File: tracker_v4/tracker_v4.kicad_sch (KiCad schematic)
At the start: 16 parts, among them J2 P70-7000045, J3 P70-7000045, U1 XIAO-ESP32-DIP, U2 LIS3DH, U4 INA226AIDGSR

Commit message: starting v4
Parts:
- removed J2, J3: P70-7000045, P70_7000045:HARWIN_P70-7000045, symbol P70-7000045:P70-7000045
- removed U1: XIAO-ESP32-DIP, Seeed_Studio_XIAO_Series:XIAO-ESP32-C6-DIP, symbol Seeed_Studio_XIAO_Series:XIAO-ESP32-C6-SMD
- added C?: 1u, symbol Device:C
- added R?: 10k, Resistor_SMD:R_0603_1608Metric, symbol Device:R
- added U?: ESP32-C6-MINI-1-N4, ESP32-C6-MINI-1-N4:XCVR_ESP32-C6-MINI-1-N4, symbol ESP32-C6-MINI-1-N4:ESP32-C6-MINI-1-N4
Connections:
- net 3v3: now also U?.3 (3V3)
- net GND: now also C?.2, U?.1 (GND1), U?.11 (GND1), U?.14 (GND1), U?.2 (GND1), U?.36 (GND1), U?.37 (GND1), U?.38 (GND1), U?.39 (GND1), U?.40 (GND1), U?.41 (GND1), U?.42 (GND1), U?.43 (GND1), U?.44 (GND1), U?.45 (GND1), U?.46 (GND1), U?.47 (GND2), U?.48 (GND2), U?.49_1 (GND2), U?.49_2 (GND2), U?.49_3 (GND2), U?.49_4 (GND2), U?.49_5 (GND2), U?.49_6 (GND2), U?.49_7 (GND2), U?.49_8 (GND2), U?.49_9 (GND2), U?.50 (GND2), U?.51 (GND2), U?.52 (GND2), U?.53 (GND2)
- net at TP5.1, U2.11 (INT1): now also R?.2
- new net: C?.1, R?.1, U?.8 (EN)
- new net: U?.21 (NC), U?.32 (NC), U?.33 (NC), U?.34 (NC), U?.35 (NC), U?.4 (NC), U?.7 (NC)
- no-connect marks 21 -> 4
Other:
- sheet Charging_and_Battery ports: added USB_DM, USB_DP; removed none

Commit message: added some stuff to schematic
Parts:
- added C?: 10u, symbol Device:C
- added IC?: RT9080-33GJ5, RT9080-33GJ5:SOT94P280X100-5N, symbol RT9080-33GJ5:RT9080-33GJ5
- added R11: 10k, symbol Device:R
- added R?: 4.7k, Resistor_SMD:R_0603_1608Metric, symbol Device:R
- added SW?: SW_Push, symbol Switch:SW_Push
- gave numbers to parts that had none: 3
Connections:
- net 3v3: now also R12.2, TP5.1, IC?.5 (VOUT), R11.1, R?.1
- net GND: now also C?.2, IC?.2 (GND), IC?.4 (SNS), SW?.1
- net SCL: now also U1.29 (IO23)
- net SDA: now also U1.28 (IO22)
- net INA226_ALERT: now reaches U4.3 (Alert)
- net INA226_ALERT: now also U1.12 (IO0), R?.2
- net USB_DM: now reaches U1.17 (IO12)
- net USB_DP: now reaches U1.18 (IO13)
- net at U1.22 (IO8): now also R11.2
- net at U1.23 (IO9): now also SW?.2
- net LIS3DH_INT1: now reaches U1.5 (IO2)
- net LIS3DH_INT1: now also U2.11 (INT1)
- net Shunt_Output renamed SHUNT_OUTPUT
- net SHUNT_OUTPUT: now also C?.1, IC?.1 (VIN), IC?.3 (EN)
- no-connect marks 4 -> 18
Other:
- moved on the sheet: C4, TP3, TP4, TP5, U1

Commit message: found changed netlist
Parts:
- gave numbers to parts that had none: 4
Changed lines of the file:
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@@
 		(dnp no)
 		(fields_autoplaced yes)
-		(property "Reference" "R?"
+		(property "Reference" "R13"
 			(at 111.76 38.0999 0)
 			(show_name no)
@@
 			(project "tracker_v4"
 				(path "/0704e846-b6bf-4206-baa8-1088b529855e"
-					(reference "R?")
+					(reference "R13")
 					(unit 1)
 				)
@@
 		(dnp no)
 		(fields_autoplaced yes)
-		(property "Reference" "C?"
+		(property "Reference" "C8"
 			(at 31.75 102.8699 0)
 			(show_name no)
@@
 			(project "tracker_v4"
 				(path "/0704e846-b6bf-4206-baa8-1088b529855e"
-					(reference "C?")
+					(reference "C8")
 					(unit 1)
 				)
@@
 		(dnp no)
 		(fields_autoplaced yes)
-		(property "Reference" "IC?"
+		(property "Reference" "IC1"
 			(at 53.34 87.63 0)
 			(show_name no)
@@
 			(project "tracker_v4"
 				(path "/0704e846-b6bf-4206-baa8-1088b529855e"
-					(reference "IC?")
+					(reference "IC1")
 					(unit 1)
 				)
@@
 		(dnp no)
 		(fields_autoplaced yes)
-		(property "Reference" "SW?"
+		(property "Reference" "SW1"
 			(at 146.05 106.6799 90)
 			(show_name no)
@@
 			(project "tracker_v4"
 				(path "/0704e846-b6bf-4206-baa8-1088b529855e"
-					(reference "SW?")
-					(unit 1)
-				)
+					(reference "SW1")
+					(unit 1)
+				)

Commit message: m
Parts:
- added C9: 22u, symbol Device:C
- added SW2: SW_Push, Button_Switch_SMD:Nidec_Copal_CAS-120A, symbol Switch:SW_Push
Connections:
- net 3v3: now also C9.2
- net GND: now also C9.1; no longer IC1.4 (SNS)
- net at R12.1, U1.8 (EN): now also SW2.1; no longer C4.1
- new net: C4.1, SW2.2
- no-connect marks 18 -> 19

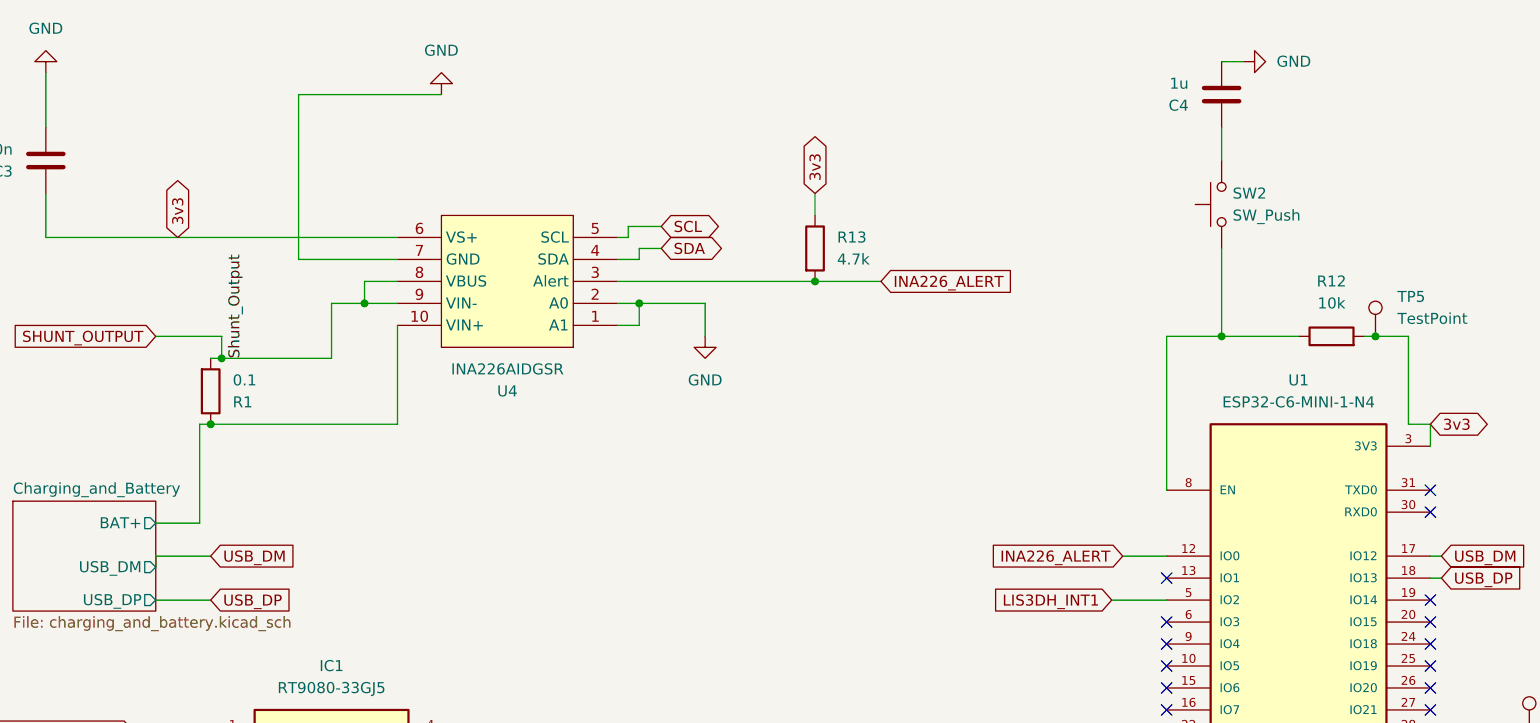
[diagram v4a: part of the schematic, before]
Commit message: added diodes
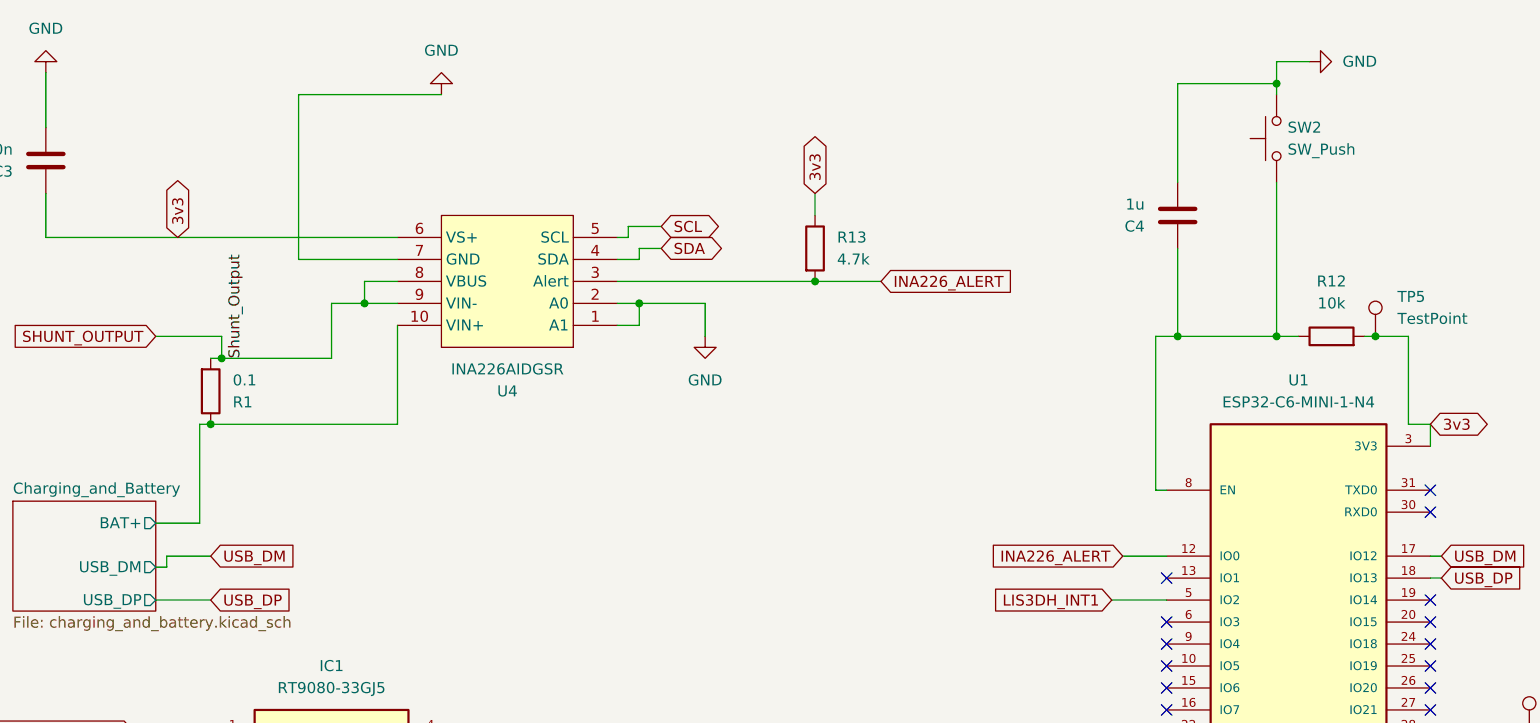
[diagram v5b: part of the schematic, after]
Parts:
- C2: footprint Capacitor_SMD:C_0603_1608Metric -> Capacitor_SMD:C_0805_2012Metric
- C4: footprint (none) -> Capacitor_SMD:C_0603_1608Metric
- C8: footprint (none) -> Capacitor_SMD:C_0201_0603Metric
- C9: footprint (none) -> Capacitor_SMD:C_1206_3216Metric
- R11: footprint (none) -> Resistor_SMD:R_0603_1608Metric
- SW1: footprint (none) -> Button_Switch_SMD:SW_Push_1P1T_NO_CK_KMR2
- SW2: footprint Button_Switch_SMD:Nidec_Copal_CAS-120A -> Button_Switch_SMD:SW_Push_1P1T_NO_CK_KMR2
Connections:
- net GND: now also SW2.2
- net at C4.1: now also R12.1, SW2.1, U1.8 (EN); no longer SW2.2
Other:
- moved on the sheet: C4, SW2
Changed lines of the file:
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@@
 	)
 	(junction
-		(at 156.21 49.53)
+		(at 173.99 49.53)
 		(diameter 0)
 		(color 0 0 0 0)
 	)
 	(junction
-		(at 173.99 49.53)
+		(at 27.94 113.03)
 		(diameter 0)
 		(color 0 0 0 0)
 	)
 	(junction
-		(at 27.94 113.03)
+		(at 196.85 101.6)
 		(diameter 0)
 		(color 0 0 0 0)
 	)
 	(junction
-		(at 196.85 101.6)
+		(at 162.56 20.32)
 		(diameter 0)
 		(color 0 0 0 0)
@@
 	)
 	(junction
+		(at 162.56 49.53)
+		(diameter 0)
+		(color 0 0 0 0)
+	)
+	(junction
 		(at 224.79 76.2)
 		(diameter 0)
@@
 	)
 	(junction
+		(at 151.13 49.53)
+		(diameter 0)
+		(color 0 0 0 0)
+	)
+	(junction
 		(at 88.9 45.72)
 		(diameter 0)
@@
 	(wire
 		(pts
+			(xy 162.56 17.78) (xy 162.56 20.32)
+		)
+		(stroke
+			(width 0)
+			(type default)
+		)
+	)
+	(wire
+		(pts
 			(xy 40.64 52.07) (xy 53.34 52.07)
 		)
@@
 	(wire
 		(pts
+			(xy 151.13 49.53) (xy 162.56 49.53)
+		)
+		(stroke
+			(width 0)
+			(type default)
+		)
+	)
+	(wire
+		(pts
 			(xy 31.75 99.06) (xy 31.75 95.25)
 		)
@@
 	(wire
 		(pts
+			(xy 151.13 31.75) (xy 151.13 20.32)
+		)
+		(stroke
+			(width 0)
+			(type default)
+		)
+	)
+	(wire
+		(pts
 			(xy 200.66 101.6) (xy 196.85 101.6)
 		)
@@
 	(wire
 		(pts
+			(xy 162.56 31.75) (xy 162.56 49.53)
+		)
+		(stroke
+			(width 0)
+			(type default)
+		)
+	)
+	(wire
+		(pts
 			(xy 57.15 45.72) (xy 60.96 45.72)
 		)
@@
 	(wire
 		(pts
+			(xy 148.59 49.53) (xy 151.13 49.53)
+		)
+		(stroke
+			(width 0)
+			(type default)
+		)
+	)
+	(wire
+		(pts
 			(xy 209.55 76.2) (xy 219.71 76.2)
 		)
@@
 	(wire
 		(pts
-			(xy 86.36 48.26) (xy 88.9 48.26)
+			(xy 34.29 76.2) (xy 34.29 74.93)
 		)
 		(stroke
@@
 	(wire
 		(pts
-			(xy 227.33 97.79) (xy 222.25 97.79)
+			(xy 86.36 48.26) (xy 88.9 48.26)
 		)
 		(stroke
@@
 	(wire
 		(pts
-			(xy 149.86 49.53) (xy 156.21 49.53)
+			(xy 227.33 97.79) (xy 222.25 97.79)
 		)
 		(stroke
@@
 	(wire
 		(pts
-			(xy 149.86 49.53) (xy 149.86 67.31)
-		)
-		(stroke
-			(width 0)
-			(type default)
-		)
-	)
-	(wire
-		(pts
 			(xy 243.84 58.42) (xy 243.84 64.77)
 		)
@@
 	(wire
 		(pts
-			(xy 33.02 74.93) (xy 33.02 76.2)
+			(xy 60.96 59.69) (xy 60.96 48.26)
 		)
 		(stroke
@@
 	(wire
 		(pts
-			(xy 60.96 59.69) (xy 60.96 48.26)
+			(xy 162.56 20.32) (xy 162.56 21.59)
 		)
 		(stroke
@@
 	(wire
 		(pts
-			(xy 156.21 39.37) (xy 156.21 49.53)
+			(xy 227.33 90.17) (xy 224.79 90.17)
 		)
 		(stroke
@@
 	(wire
 		(pts
-			(xy 227.33 90.17) (xy 224.79 90.17)
+			(xy 250.19 114.3) (xy 224.79 114.3)
 		)
 		(stroke
@@
 	(wire
 		(pts
-			(xy 250.19 114.3) (xy 224.79 114.3)
+			(xy 143.51 80.01) (xy 149.86 80.01)
 		)
 		(stroke
@@
 	(wire
 		(pts
-			(xy 143.51 80.01) (xy 149.86 80.01)
+			(xy 242.57 74.93) (xy 242.57 77.47)
 		)
 		(stroke
@@
 	(wire
 		(pts
-			(xy 242.57 74.93) (xy 242.57 77.47)
+			(xy 151.13 39.37) (xy 151.13 49.53)
 		)
 		(stroke
@@
 	(wire
 		(pts
-			(xy 156.21 25.4) (xy 156.21 29.21)
+			(xy 20.32 38.1) (xy 20.32 33.02)
 		)
 		(stroke
@@
 	(wire
 		(pts
-			(xy 20.32 38.1) (xy 20.32 33.02)
+			(xy 53.34 45.72) (xy 57.15 45.72)
 		)
 		(stroke
@@
 	(wire
 		(pts
-			(xy 53.34 45.72) (xy 57.15 45.72)
+			(xy 240.03 139.7) (xy 240.03 105.41)
 		)
 		(stroke
@@
 	(wire
 		(pts
-			(xy 240.03 139.7) (xy 240.03 105.41)
+			(xy 148.59 67.31) (xy 149.86 67.31)
 		)
 		(stroke
@@
 	(wire
 		(pts
+			(xy 34.29 74.93) (xy 39.37 74.93)
+		)
+		(stroke
+			(width 0)
+			(type default)
+		)
+	)
+	(wire
+		(pts
 			(xy 261.62 123.19) (xy 261.62 114.3)
 		)
@@
 	(wire
 		(pts
-			(xy 158.75 17.78) (xy 156.21 17.78)
+			(xy 162.56 17.78) (xy 166.37 17.78)
 		)
 		(stroke
@@
 	(wire
 		(pts
+			(xy 151.13 20.32) (xy 162.56 20.32)
+		)
+		(stroke
+			(width 0)
+			(type default)
+		)
+	)
+	(wire
+		(pts
 			(xy 87.63 36.83) (xy 91.44 36.83)
 		)
@@
 	(wire
 		(pts
-			(xy 39.37 74.93) (xy 33.02 74.93)
+			(xy 34.29 76.2) (xy 33.02 76.2)
 		)
 		(stroke
@@
 	(wire
 		(pts
-			(xy 156.21 49.53) (xy 165.1 49.53)
+			(xy 148.59 49.53) (xy 148.59 67.31)
 		)
 		(stroke
@@
 	(wire
 		(pts
+			(xy 162.56 49.53) (xy 165.1 49.53)
+		)
+		(stroke
+			(width 0)
+			(type default)
+		)
+	)
+	(wire
+		(pts
 			(xy 39.37 59.69) (xy 60.96 59.69)
 		)
@@
 			)
 		)
-		(property "Footprint" "Capacitor_SMD:C_0603_1608Metric"
+		(property "Footprint" "Capacitor_SMD:C_0805_2012Metric"
 			(at 234.6452 72.39 0)
 			(hide yes)
@@
 	(symbol
 		(lib_id "power:GND")
-		(at 158.75 17.78 90)
+		(at 166.37 17.78 90)
 		(unit 1)
 		(body_style 1)
@@
 		(fields_autoplaced yes)
 		(property "Reference" "#PWR010"
-			(at 165.1 17.78 0)
+			(at 172.72 17.78 0)
 			(hide yes)
 			(show_name no)
@@
 		)
 		(property "Value" "GND"
-			(at 162.56 17.7801 90)
+			(at 170.18 17.7801 90)
 			(show_name no)
 			(do_not_autoplace no)
@@
 		)
 		(property "Footprint" ""
-			(at 158.75 17.78 0)
+			(at 166.37 17.78 0)
 			(hide yes)
 			(show_name no)
@@
 		)
 		(property "Datasheet" ""
-			(at 158.75 17.78 0)
+			(at 166.37 17.78 0)
 			(hide yes)
 			(show_name no)
@@
 		)
 		(property "Description" "Power symbol creates a global label with name \"GND\" , ground"
-			(at 158.75 17.78 0)
+			(at 166.37 17.78 0)
 			(hide yes)
 			(show_name no)
@@
 			)
 		)
-		(property "Footprint" ""
+		(property "Footprint" "Capacitor_SMD:C_0201_0603Metric"
 			(at 28.9052 107.95 0)
 			(hide yes)
@@
 			)
 		)
-		(property "Footprint" ""
+		(property "Footprint" "Resistor_SMD:R_0603_1608Metric"
 			(at 138.938 106.68 90)
 			(hide yes)
@@
 			)
 		)
-		(property "Footprint" ""
+		(property "Footprint" "Capacitor_SMD:C_1206_3216Metric"
 			(at 220.6752 66.04 0)
 			(hide yes)
@@
 			(at 219.71 62.23 0)
 			(hide yes)
-			(show_name no)
+			(show_name yes)
 			(do_not_autoplace no)
 			(effects
@@
 	(symbol
 		(lib_id "Device:C")
-		(at 156.21 21.59 180)
+		(at 151.13 35.56 180)
 		(unit 1)
 		(body_style 1)
@@
 		(fields_autoplaced yes)
 		(property "Reference" "C4"
-			(at 152.4 22.8601 0)
+			(at 147.32 36.8301 0)
 			(show_name no)
 			(do_not_autoplace no)
@@
 		)
 		(property "Value" "1u"
-			(at 152.4 20.3201 0)
+			(at 147.32 34.2901 0)
 			(show_name no)
 			(do_not_autoplace no)
@@
 			)
 		)
-		(property "Footprint" ""
-			(at 155.2448 17.78 0)
+		(property "Footprint" "Capacitor_SMD:C_0603_1608Metric"
+			(at 150.1648 31.75 0)
 			(hide yes)
 			(show_name no)
@@
 		)
 		(property "Datasheet" ""
-			(at 156.21 21.59 0)
+			(at 151.13 35.56 0)
 			(hide yes)
 			(show_name no)
@@
 		)
 		(property "Description" "Unpolarized capacitor"
-			(at 156.21 21.59 0)
+			(at 151.13 35.56 0)
 			(hide yes)
 			(show_name no)
@@
 			)
 		)
-		(property "Footprint" ""
+		(property "Footprint" "Button_Switch_SMD:SW_Push_1P1T_NO_CK_KMR2"
 			(at 139.7 107.95 0)
 			(hide yes)
@@
 	(symbol
 		(lib_id "Switch:SW_Push")
-		(at 156.21 34.29 90)
+		(at 162.56 26.67 90)
 		(unit 1)
 		(body_style 1)
@@
 		(fields_autoplaced yes)
 		(property "Reference" "SW2"
-			(at 157.48 33.0199 90)
+			(at 163.83 25.3999 90)
 			(show_name no)
 			(do_not_autoplace no)
@@
 		)
 		(property "Value" "SW_Push"
-			(at 157.48 35.5599 90)
+			(at 163.83 27.9399 90)
 			(show_name no)
 			(do_not_autoplace no)
@@
 			)
 		)
-		(property "Footprint" "Button_Switch_SMD:Nidec_Copal_CAS-120A"
-			(at 151.13 34.29 0)
+		(property "Footprint" "Button_Switch_SMD:SW_Push_1P1T_NO_CK_KMR2"
+			(at 157.48 26.67 0)
 			(hide yes)
 			(show_name no)
@@
 		)
 		(property "Datasheet" ""
-			(at 151.13 34.29 0)
+			(at 157.48 26.67 0)
 			(hide yes)
 			(show_name no)
@@
 		)
 		(property "Description" "Push button switch, generic, two pins"
-			(at 156.21 34.29 0)
+			(at 162.56 26.67 0)
 			(hide yes)
 			(show_name no)

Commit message: corrected schematic
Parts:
- C8: footprint Capacitor_SMD:C_0201_0603Metric -> Capacitor_SMD:C_0805_2012Metric
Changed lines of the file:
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@@
 			)
 		)
-		(property "Footprint" "Capacitor_SMD:C_0201_0603Metric"
+		(property "Footprint" "Capacitor_SMD:C_0805_2012Metric"
 			(at 28.9052 107.95 0)
 			(hide yes)

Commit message: jk
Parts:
- added C10, C12, C13: 100n, Capacitor_SMD:C_0603_1608Metric, symbol Device:C
- added C11: 10n, Capacitor_SMD:C_0603_1608Metric, symbol Device:C
- added R14: 1.27M, Resistor_SMD:R_0603_1608Metric, symbol Device:R
- added R15: 226k, Resistor_SMD:R_0603_1608Metric, symbol Device:R
- added R16: 1M, Resistor_SMD:R_0603_1608Metric, symbol Device:R
- added U7: TPS3899DL01DSER, DSE0006A-IPC_A, symbol 2026-10-23_10-32-17:PTPS3899DL01DSER
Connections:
- net GND: now also C10.2, C11.2, C12.2, C13.2, R15.2, U7.3 (GND)
- net SHUNT_OUTPUT: now also C10.1, R14.1, R16.1, U7.4 (VDD); no longer IC1.3 (EN)
- new net: C13.1, U7.1 (CTR)
- new net: C12.1, U7.2 (CTS)
- new net LDO_EN: IC1.3 (EN), R16.2, U7.6 (RESET_N)
- new net UVLO_SENSE: C11.1, R14.2, R15.1, U7.5 (SENSE)

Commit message: jkd
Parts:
- removed IC1: RT9080-33GJ5, RT9080-33GJ5:SOT94P280X100-5N, symbol RT9080-33GJ5:RT9080-33GJ5
- added C14: 22u, Capacitor_SMD:C_1206_3216Metric, symbol Device:C
- added C16, C18: 10u, Capacitor_SMD:C_0805_2012Metric, symbol Device:C
- added C17: 100n, Capacitor_SMD:C_0603_1608Metric, symbol Device:C
- added L1: 1.0u, Inductor_SMD:L_Coilcraft_XxL4020, symbol Device:L
- added R17: 1M, Resistor_SMD:R_0603_1608Metric, symbol Device:R
- added R18: 180k, Resistor_SMD:R_0603_1608Metric, symbol Device:R
- added R22: 10k, Resistor_SMD:R_0603_1608Metric, symbol Device:R
- added U5: TPS63020, TPS63020:TPS63020, symbol TPS63020:TPS63020
- C8: value 10u -> 22u; footprint Capacitor_SMD:C_0805_2012Metric -> Capacitor_SMD:C_1206_3216Metric
- R14: value 1.27M -> 499k
- R15: value 226k -> 100k
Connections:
- net 3v3: now also C8.1, C14.2, R17.1, U5.PIN4 (VOUT), U5.PIN5 (VOUT)
- net GND: now also C14.1, C16.1, C17.1, C18.1, R18.2, R22.2, U5.PAD1 (PGND), U5.PAD2 (PGND), U5.PAD3 (PGND), U5.PAD4 (PGND), U5.PAD5 (PGND), U5.PAD6 (PGND), U5.PAD7 (PGND), U5.PAD8 (PGND), U5.PIN2 (GND)
- net SHUNT_OUTPUT: now also C16.2, C17.2, C18.2, U5.PIN1 (VINA), U5.PIN10 (VIN), U5.PIN11 (VIN); no longer C8.1
- net BUCK_SYNC: now reaches U1.9 (IO4)
- net BUCK_SYNC: now also R22.1, U5.PIN13 (SYNC)
- net Charging_and_Battery/BAT+ renamed POWER_OUT
- net LDO_EN renamed BUCK_EN
- net BUCK_EN: now also U5.PIN12 (EN)
- new net: R17.2, R18.1, U5.PIN3 (FB)
- new net: L1.1, U5.PIN8 (L1), U5.PIN9 (L1)
- new net: L1.2, U5.PIN6 (L2), U5.PIN7 (L2)
- no-connect marks 19 -> 18
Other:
- sheet Charging_and_Battery ports: added POWER_OUT; removed BAT+
- note added: "Regulator"
- note added: "Supervisor"
